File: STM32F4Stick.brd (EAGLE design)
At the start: 46.7 x 25.9 mm, 46 parts, among them U1 MIC5219 3.3V, U2 USD-SOCKETNEW

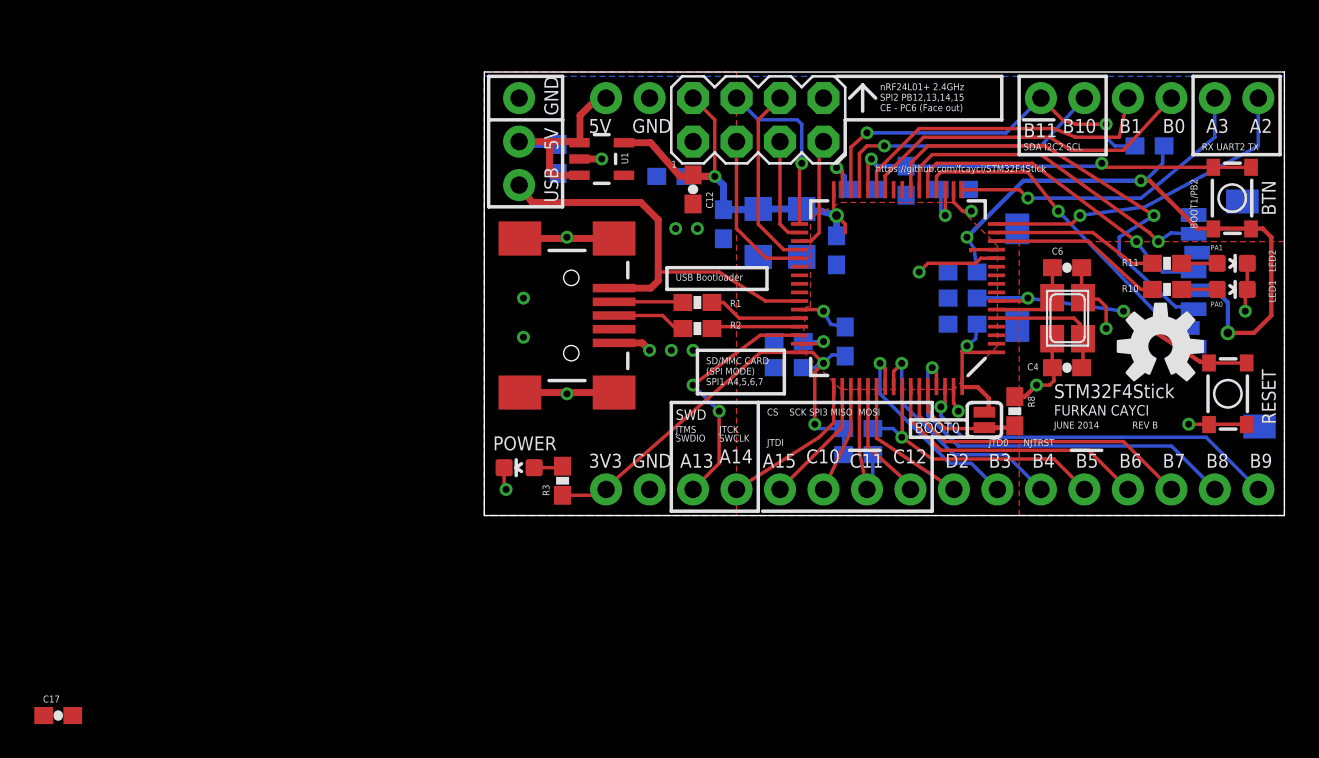
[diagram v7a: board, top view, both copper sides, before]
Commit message: V2 RevB final. Finalize stm32f401 support on version 2 board.
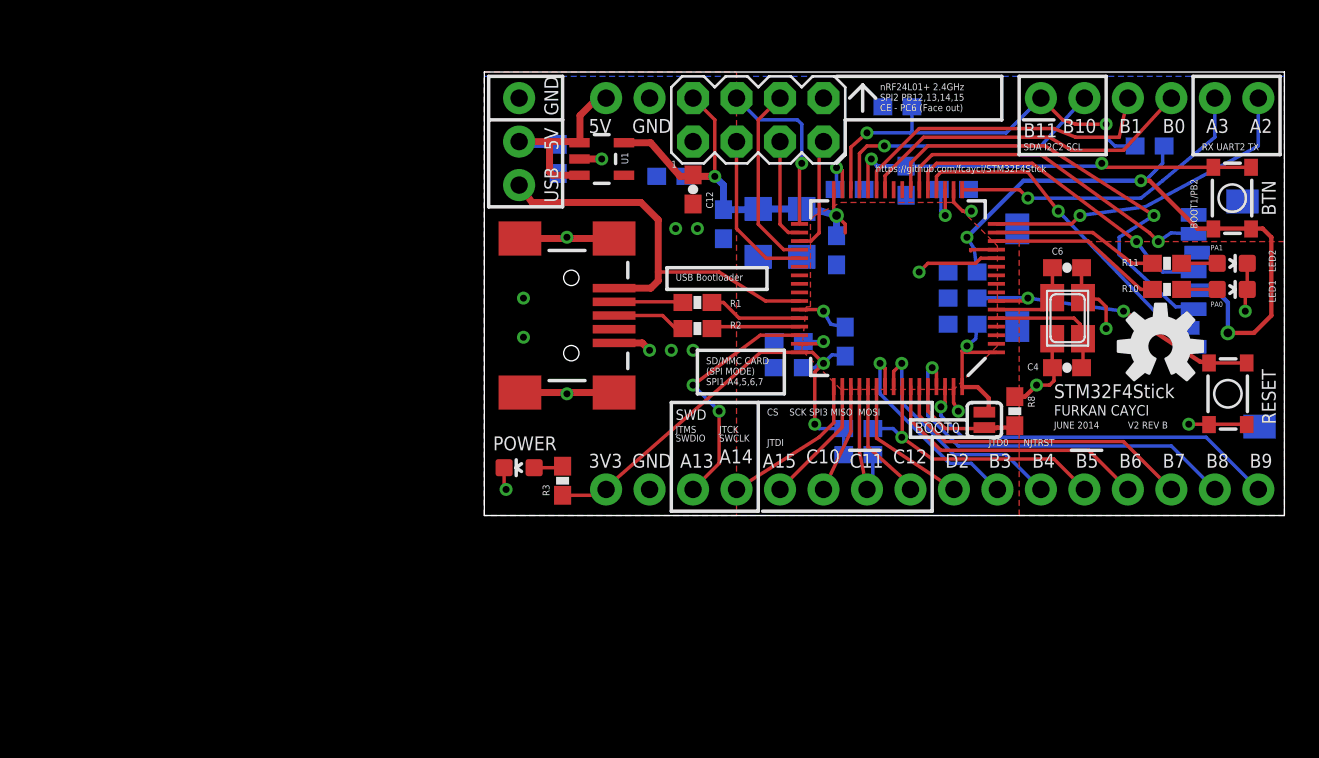
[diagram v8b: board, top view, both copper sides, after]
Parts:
- moved C17 60.6 mm to (24.1, 23.9), flipped to the bottom
- moved C5 0.76 mm to (21.3, 19.1)
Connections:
- net BOOT1: now also S2.3
- net GND: now also S1.2
- net NRST: now also S1.3
- net VCC: now also S2.2
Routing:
- net P30: track 21.8 -> 23.3 mm
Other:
- board text added: "For STM32F401 0-ohm res"
- board text added: "STM32F401 only 4.7uF <1ohm ESR"
- board text added: "V2 REV B"
- board text removed: "REV B"
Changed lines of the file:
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@@
 <layer number="23" name="tOrigins" color="15" fill="1" visible="yes" active="yes"/>
 <layer number="24" name="bOrigins" color="15" fill="1" visible="yes" active="yes"/>
-<layer number="25" name="tNames" color="7" fill="1" visible="yes" active="yes"/>
+<layer number="25" name="tNames" color="7" fill="1" visible="no" active="yes"/>
 <layer number="26" name="bNames" color="7" fill="1" visible="yes" active="yes"/>
 <layer number="27" name="tValues" color="7" fill="1" visible="no" active="yes"/>
@@
 <text x="33.274" y="5.842" size="0.6096" layer="21" ratio="15">FURKAN CAYCI</text>
 <text x="33.274" y="5.08" size="0.4064" layer="21" ratio="15">JUNE 2014</text>
-<text x="37.846" y="5.08" size="0.4064" layer="21" ratio="15">REV B</text>
+<text x="37.592" y="5.08" size="0.4064" layer="21" ratio="15">V2 REV B</text>
 <wire x1="12.446" y1="9.652" x2="17.526" y2="9.652" width="0.2032" layer="21"/>
 <wire x1="17.526" y1="9.652" x2="17.526" y2="7.112" width="0.2032" layer="21"/>
@@
 <wire x1="24.892" y1="5.588" x2="24.892" y2="4.572" width="0.2032" layer="21"/>
 <wire x1="24.892" y1="4.572" x2="26.162" y2="4.572" width="0.2032" layer="21"/>
+<wire x1="22.098" y1="22.86" x2="22.098" y2="25.146" width="0.2032" layer="22"/>
+<wire x1="22.098" y1="25.146" x2="30.48" y2="25.146" width="0.2032" layer="22"/>
+<wire x1="30.48" y1="25.146" x2="30.48" y2="22.86" width="0.2032" layer="22"/>
+<wire x1="30.48" y1="22.86" x2="22.098" y2="22.86" width="0.2032" layer="22"/>
+<text x="29.972" y="23.368" size="0.3048" layer="22" font="vector" ratio="15" rot="MR0">STM32F401 only
+4.7uF &lt;1ohm ESR</text>
+<wire x1="19.304" y1="19.812" x2="23.622" y2="19.812" width="0.2032" layer="22"/>
+<wire x1="23.622" y1="19.812" x2="23.622" y2="17.78" width="0.2032" layer="22"/>
+<wire x1="23.622" y1="17.78" x2="25.908" y2="17.78" width="0.2032" layer="22"/>
+<wire x1="25.908" y1="17.78" x2="25.908" y2="16.51" width="0.2032" layer="22"/>
+<wire x1="25.908" y1="16.51" x2="21.59" y2="16.51" width="0.2032" layer="22"/>
+<wire x1="21.59" y1="16.51" x2="21.59" y2="18.288" width="0.2032" layer="22"/>
+<wire x1="21.59" y1="18.288" x2="19.812" y2="18.288" width="0.2032" layer="22"/>
+<wire x1="19.812" y1="18.288" x2="19.812" y2="18.542" width="0.2032" layer="22"/>
+<wire x1="19.812" y1="18.542" x2="19.304" y2="19.05" width="0.2032" layer="22"/>
+<wire x1="19.304" y1="19.05" x2="19.304" y2="19.812" width="0.2032" layer="22"/>
+<text x="25.654" y="16.764" size="0.3048" layer="22" font="vector" ratio="15" rot="MR0">For STM32F401
+0-ohm res</text>
 </plain>
 <attributes>
@@
 <attribute name="VALUE" x="27.1608125" y="10.28239375" size="0.4064" layer="27" rot="R90"/>
 </element>
-<element name="C5" library="SparkFun-Capacitors" package="0603-CAP" value="2.2uF" x="22.098" y="19.05" rot="MR180">
-<attribute name="PROD_ID" value="CAP-07888" x="53.848" y="64.77" size="1.778" layer="28" rot="MR180" display="off"/>
+<element name="C5" library="SparkFun-Capacitors" package="0603-CAP" value="2.2uF" x="21.336" y="19.05" rot="MR180">
+<attribute name="PROD_ID" value="CAP-07888" x="53.086" y="64.77" size="1.778" layer="28" rot="MR180" display="off"/>
 </element>
 <element name="C15" library="SparkFun-Capacitors" package="0603-CAP" value="2.2uF" x="17.78" y="10.16" smashed="yes" rot="MR0">
@@
 <attribute name="VALUE" x="11.049" y="20.066" size="0.4064" layer="27" font="vector" rot="R270"/>
 </element>
-<element name="C17" library="SparkFun-Capacitors" package="0603-CAP" value="4.7uF" x="-24.892" y="-11.684">
-<attribute name="PROD_ID" value="CAP-08280" x="-24.892" y="-11.684" size="1.778" layer="27" ratio="15" display="off"/>
+<element name="C17" library="SparkFun-Capacitors" package="0603-CAP" value="4.7uF" x="24.13" y="23.876" rot="MR0">
+<attribute name="PROD_ID" value="CAP-08280" x="24.13" y="23.876" size="1.778" layer="28" ratio="15" rot="MR0" display="off"/>
 </element>
 </elements>
@@
 <wire x1="12.192" y1="24.384" x2="13.462" y2="23.114" width="0.2032" layer="1"/>
 <wire x1="13.462" y1="23.114" x2="13.462" y2="19.812" width="0.2032" layer="1"/>
+<contactref element="S2" pad="2"/>
 </signal>
 <signal name="GND">
@@
 <contactref element="C12" pad="2"/>
 <contactref element="C17" pad="2"/>
-<wire x1="1.155" y1="1.639" x2="-24.042" y2="-11.684" width="0" layer="19" extent="1-1"/>
+<contactref element="S1" pad="2"/>
 </signal>
 <signal name="N$10">
@@
 <wire x1="41.822" y1="8.978" x2="42.33" y2="8.978" width="0.254" layer="1"/>
 <wire x1="42.33" y1="8.978" x2="42.334" y2="8.974" width="0.254" layer="1"/>
+<contactref element="S1" pad="3"/>
 </signal>
 <signal name="USB_DP">
@@
 <wire x1="20.9108125" y1="20.1488125" x2="20.574" y2="20.32" width="0.2032" layer="1"/>
 <via x="20.574" y="20.32" extent="1-16" drill="0.4064"/>
-<wire x1="21.082" y1="19.216" x2="21.248" y2="19.05" width="0.2032" layer="16"/>
-<wire x1="21.082" y1="19.216" x2="21.082" y2="19.812" width="0.2032" layer="16"/>
-<wire x1="21.082" y1="19.812" x2="20.574" y2="20.32" width="0.2032" layer="16"/>
+<wire x1="20.574" y1="19.216" x2="20.486" y2="19.05" width="0.2032" layer="16"/>
+<wire x1="20.574" y1="19.216" x2="20.574" y2="20.32" width="0.2032" layer="16"/>
 </signal>
 <signal name="P17">
@@
 <wire x1="44.788" y1="20.342" x2="36.3" y2="20.342" width="0.2032" layer="1"/>
 <wire x1="36.3" y1="20.342" x2="36.068" y2="20.574" width="0.2032" layer="1"/>
+<contactref element="S2" pad="3"/>
 </signal>
 <signal name="5V">
@@
 <wire x1="21.4108125" y1="21.5151875" x2="22.352" y2="22.352" width="0.2032" layer="1"/>
 <via x="22.352" y="22.352" extent="1-16" drill="0.4064"/>
-<wire x1="22.352" y1="22.352" x2="30.48" y2="22.352" width="0.2032" layer="16"/>
+<wire x1="22.352" y1="22.352" x2="24.892" y2="22.352" width="0.2032" layer="16"/>
+<wire x1="24.892" y1="22.352" x2="30.48" y2="22.352" width="0.2032" layer="16"/>
 <wire x1="30.48" y1="22.352" x2="32.512" y2="24.384" width="0.2032" layer="16"/>
 <contactref element="R5" pad="1"/>
@@
 <contactref element="JP3" pad="1"/>
 <contactref element="C17" pad="1"/>
-<wire x1="-25.742" y1="-11.684" x2="21.4108125" y2="19.03239375" width="0" layer="19" extent="1-1"/>
+<wire x1="24.98" y1="23.876" x2="24.98" y2="22.44" width="0.2032" layer="16"/>
+<wire x1="24.98" y1="22.44" x2="24.892" y2="22.352" width="0.2032" layer="16"/>
 </signal>
 <signal name="RF_CE">
